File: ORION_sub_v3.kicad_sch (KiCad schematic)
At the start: 74 parts, among them J1 Conn_01x02, J10 Conn_01x01, J11 Conn_01x05, J12 Conn_01x04, J2 Conn_01x03, J3 Conn_01x04, J4 Conn_01x02, J5 Conn_01x01, J6 Conn_01x04, J7 Conn_01x03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

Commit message: スイッチ変更、電源ヒューズ追加
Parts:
- added F1: Polyfuse, Fuse:Fuse_1206_3216Metric, symbol Device:Polyfuse
- SW1, SW2, SW3, SW4: footprint Button_Switch_SMD:SW_Push_1P1T_NO_CK_KMR2 -> Button_Switch_SMD:SW_Push_SPST_NO_Alps_SKRK
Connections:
- net +BATT: now also F1.1; no longer C12.1, U4.4 (EN), U4.5 (VCC)
- new net BATT_fuse: C12.1, F1.2, U4.4 (EN), U4.5 (VCC)
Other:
- note added: "要修正"
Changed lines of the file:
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@@
   (junction (at 62.23 163.83) (diameter 0) (color 0 0 0 0)
   )
-  (junction (at 54.61 168.91) (diameter 0) (color 0 0 0 0)
-  )
   (junction (at 49.53 115.57) (diameter 0) (color 0 0 0 0)
   )
@@
     (stroke (width 0) (type default) (color 0 0 0 0))
   )
+  (wire (pts (xy 48.26 167.64) (xy 48.26 168.91))
+    (stroke (width 0) (type default) (color 0 0 0 0))
+  )
   (wire (pts (xy 81.28 173.99) (xy 88.9 173.99))
     (stroke (width 0) (type default) (color 0 0 0 0))
@@
     (stroke (width 0) (type default) (color 0 0 0 0))
   )
+  (wire (pts (xy 31.75 137.16) (xy 38.1 137.16))
+    (stroke (width 0) (type default) (color 0 0 0 0))
+  )
   (wire (pts (xy 33.02 182.88) (xy 27.94 182.88))
     (stroke (width 0) (type default) (color 0 0 0 0))
@@
     (stroke (width 0) (type default) (color 0 0 0 0))
   )
+  (wire (pts (xy 45.72 137.16) (xy 49.53 137.16))
+    (stroke (width 0) (type default) (color 0 0 0 0))
+  )
   (wire (pts (xy 162.56 16.51) (xy 165.1 16.51))
     (stroke (width 0) (type default) (color 0 0 0 0))
@@
     (stroke (width 0) (type default) (color 0 0 0 0))
   )
+  (text "要修正" (at 123.19 198.12 0)
+    (effects (font (size 5 5)) (justify left bottom))
+  )
   (label "SW_0" (at 123.19 20.32 180)
     (effects (font (size 1.27 1.27)) (justify right bottom))
@@
     (effects (font (size 1.27 1.27)) (justify right bottom))
   )
+  (label "BATT_fuse" (at 49.53 137.16 0)
+    (effects (font (size 1.27 1.27)) (justify left bottom))
+  )
   (label "OSC_OUT" (at 236.22 20.32 0)
     (effects (font (size 1.524 1.524)) (justify left bottom))
@@
     (effects (font (size 1.27 1.27)) (justify right bottom))
   )
+  (label "BATT_fuse" (at 48.26 167.64 0)
+    (effects (font (size 1.27 1.27)) (justify left bottom))
+  )
   (label "LED_2" (at 34.29 64.77 180)
     (effects (font (size 1.524 1.524)) (justify right bottom))
@@
       (effects (font (size 1.27 1.27)) (justify right))
     )
-    (property "Footprint" "Button_Switch_SMD:SW_Push_1P1T_NO_CK_KMR2" (id 2) (at 130.81 25.4 0)
+    (property "Footprint" "Button_Switch_SMD:SW_Push_SPST_NO_Alps_SKRK" (id 2) (at 130.81 25.4 0)
       (effects (font (size 1.27 1.27)) hide)
     )
@@
       (effects (font (size 1.27 1.27)) (justify right))
     )
-    (property "Footprint" "Button_Switch_SMD:SW_Push_1P1T_NO_CK_KMR2" (id 2) (at 143.51 25.4 0)
+    (property "Footprint" "Button_Switch_SMD:SW_Push_SPST_NO_Alps_SKRK" (id 2) (at 143.51 25.4 0)
       (effects (font (size 1.27 1.27)) hide)
     )
@@
     (pin "1")
   )
+  (symbol (lib_id "Device:Polyfuse") (at 41.91 137.16 90) (unit 1)
+    (in_bom yes) (on_board yes) (fields_autoplaced)
+    (property "Reference" "F1" (id 0) (at 40.6399 134.62 0)
+      (effects (font (size 1.27 1.27)) (justify left))
+    )
+    (property "Value" "Polyfuse" (id 1) (at 43.1799 134.62 0)
+      (effects (font (size 1.27 1.27)) (justify left))
+    )
+    (property "Footprint" "Fuse:Fuse_1206_3216Metric" (id 2) (at 46.99 135.89 0)
+      (effects (font (size 1.27 1.27)) (justify left) hide)
+    )
+    (property "Datasheet" "~" (id 3) (at 41.91 137.16 0)
+      (effects (font (size 1.27 1.27)) hide)
+    )
+    (pin "1")
+    (pin "2")
+  )
   (symbol (lib_id "User:BD9G101G") (at 36.83 168.91 0) (unit 1)
     (in_bom yes) (on_board yes) (fields_autoplaced)
@@
       (effects (font (size 1.27 1.27)) (justify right))
     )
-    (property "Footprint" "Button_Switch_SMD:SW_Push_1P1T_NO_CK_KMR2" (id 2) (at 118.11 25.4 0)
+    (property "Footprint" "Button_Switch_SMD:SW_Push_SPST_NO_Alps_SKRK" (id 2) (at 118.11 25.4 0)
       (effects (font (size 1.27 1.27)) hide)
     )
@@
     (pin "1")
   )
-  (symbol (lib_id "power:+BATT") (at 54.61 168.91 0) (unit 1)
+  (symbol (lib_id "power:+BATT") (at 31.75 137.16 0) (unit 1)
     (in_bom yes) (on_board yes)
-    (property "Reference" "#PWR012" (id 0) (at 54.61 172.72 0)
+    (property "Reference" "#PWR012" (id 0) (at 31.75 140.97 0)
       (effects (font (size 1.27 1.27)) hide)
     )
-    (property "Value" "+BATT" (id 1) (at 48.26 166.37 0)
+    (property "Value" "+BATT" (id 1) (at 25.4 134.62 0)
       (effects (font (size 1.27 1.27)) (justify left))
     )
-    (property "Footprint" "" (id 2) (at 54.61 168.91 0)
+    (property "Footprint" "" (id 2) (at 31.75 137.16 0)
       (effects (font (size 1.27 1.27)) hide)
     )
-    (property "Datasheet" "" (id 3) (at 54.61 168.91 0)
+    (property "Datasheet" "" (id 3) (at 31.75 137.16 0)
       (effects (font (size 1.27 1.27)) hide)
     )
@@
     )
     (property "Value" "SW_Push" (id 1) (at 161.036 24.13 0))
-    (property "Footprint" "Button_Switch_SMD:SW_Push_1P1T_NO_CK_KMR2" (id 2) (at 167.64 24.13 0)
+    (property "Footprint" "Button_Switch_SMD:SW_Push_SPST_NO_Alps_SKRK" (id 2) (at 167.64 24.13 0)
       (effects (font (size 1.27 1.27)) hide)
     )
@@
       (reference "D10") (unit 1) (value "LED") (footprint "LED_SMD:LED_0603_1608Metric")
     )
+    (path "/42055cd1-520a-46d4-8bb1-032d7acd9f1c"
+      (reference "F1") (unit 1) (value "Polyfuse") (footprint "Fuse:Fuse_1206_3216Metric")
+    )
     (path "/b6763645-6ebb-43f8-9e23-2738718aabe3"
       (reference "J1") (unit 1) (value "Conn_01x02") (footprint "Connector_Hirose:Hirose_DF13-02P-1.25DSA_1x02_P1.25mm_Vertical")
@@
     )
     (path "/e2c39e4b-8894-40d7-8b0a-a70128ca8812"
-      (reference "SW1") (unit 1) (value "SW_Push") (footprint "Button_Switch_SMD:SW_Push_1P1T_NO_CK_KMR2")
+      (reference "SW1") (unit 1) (value "SW_Push") (footprint "Button_Switch_SMD:SW_Push_SPST_NO_Alps_SKRK")
     )
     (path "/ae53bb4e-83e0-4f31-8b54-9513ada53cca"
-      (reference "SW2") (unit 1) (value "SW_Push") (footprint "Button_Switch_SMD:SW_Push_1P1T_NO_CK_KMR2")
+      (reference "SW2") (unit 1) (value "SW_Push") (footprint "Button_Switch_SMD:SW_Push_SPST_NO_Alps_SKRK")
     )
     (path "/1c7c0e3b-07ed-4d05-9bda-8a1656c2d04b"
-      (reference "SW3") (unit 1) (value "SW_Push") (footprint "Button_Switch_SMD:SW_Push_1P1T_NO_CK_KMR2")
+      (reference "SW3") (unit 1) (value "SW_Push") (footprint "Button_Switch_SMD:SW_Push_SPST_NO_Alps_SKRK")
     )
     (path "/3fe8974f-82c8-4bf4-9d5e-55518adc24c7"
-      (reference "SW4") (unit 1) (value "SW_Push") (footprint "Button_Switch_SMD:SW_Push_1P1T_NO_CK_KMR2")
+      (reference "SW4") (unit 1) (value "SW_Push") (footprint "Button_Switch_SMD:SW_Push_SPST_NO_Alps_SKRK")
     )
     (path "/50c41588-ebff-4aa2-b689-dd60a441b123"

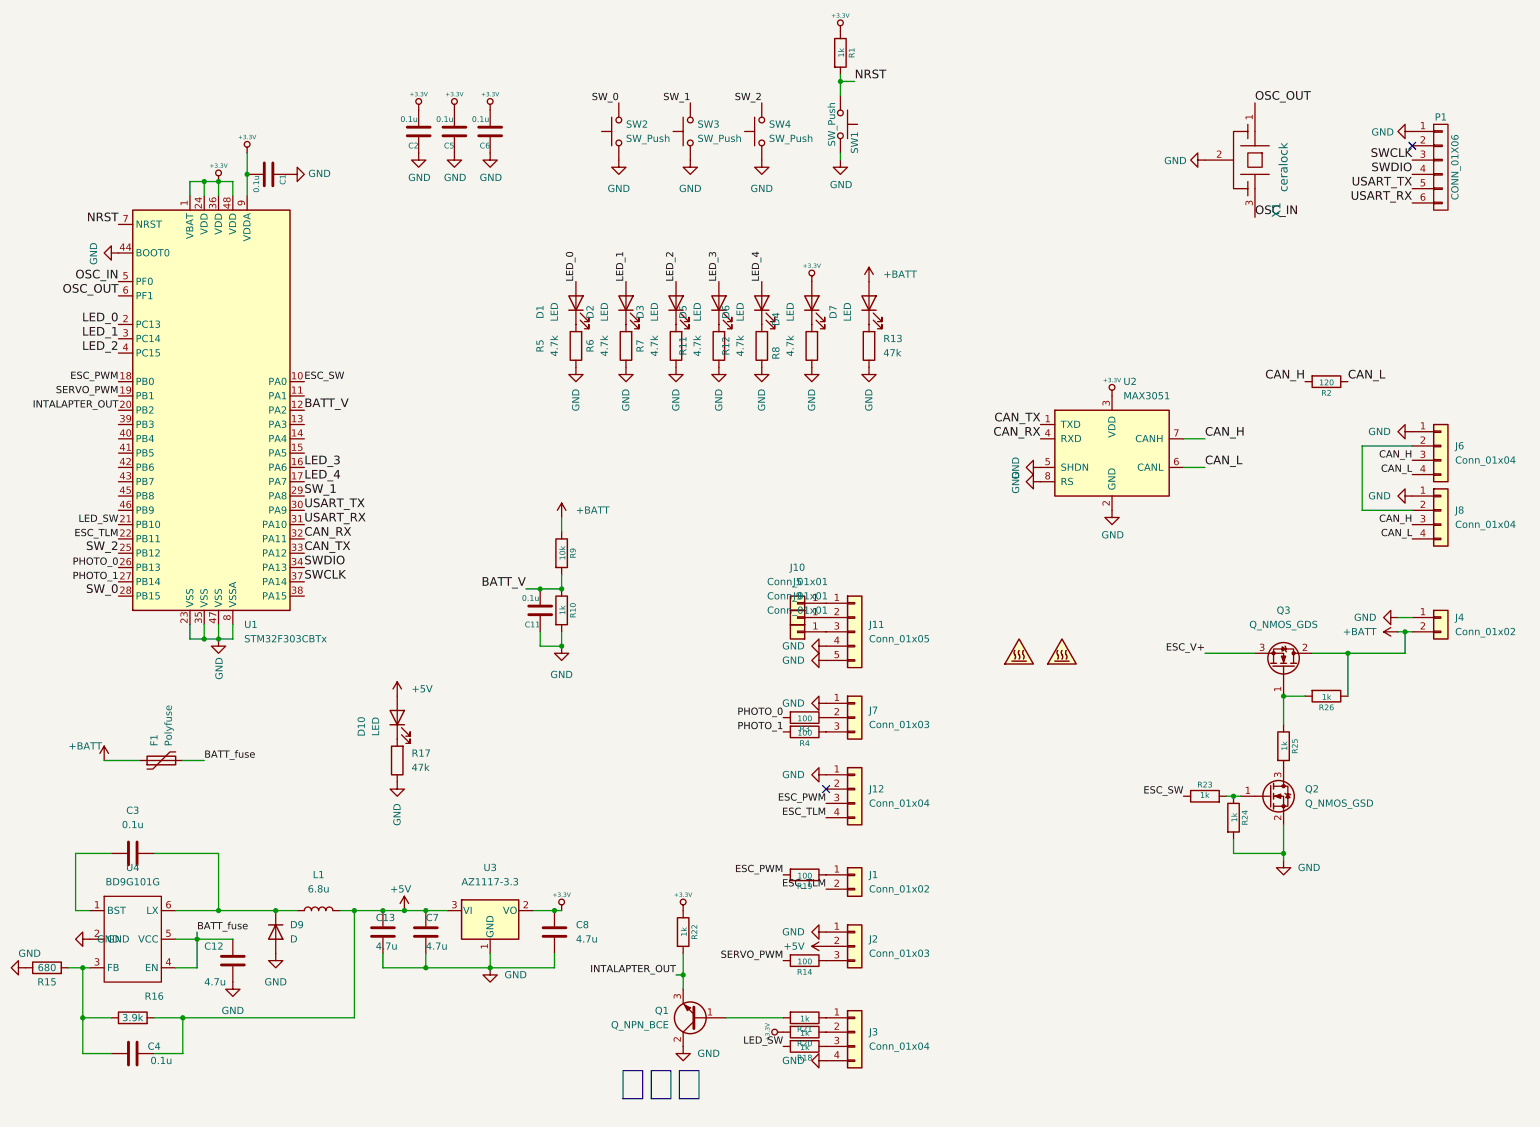
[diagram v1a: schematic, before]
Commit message: KiCAD8.0に更新
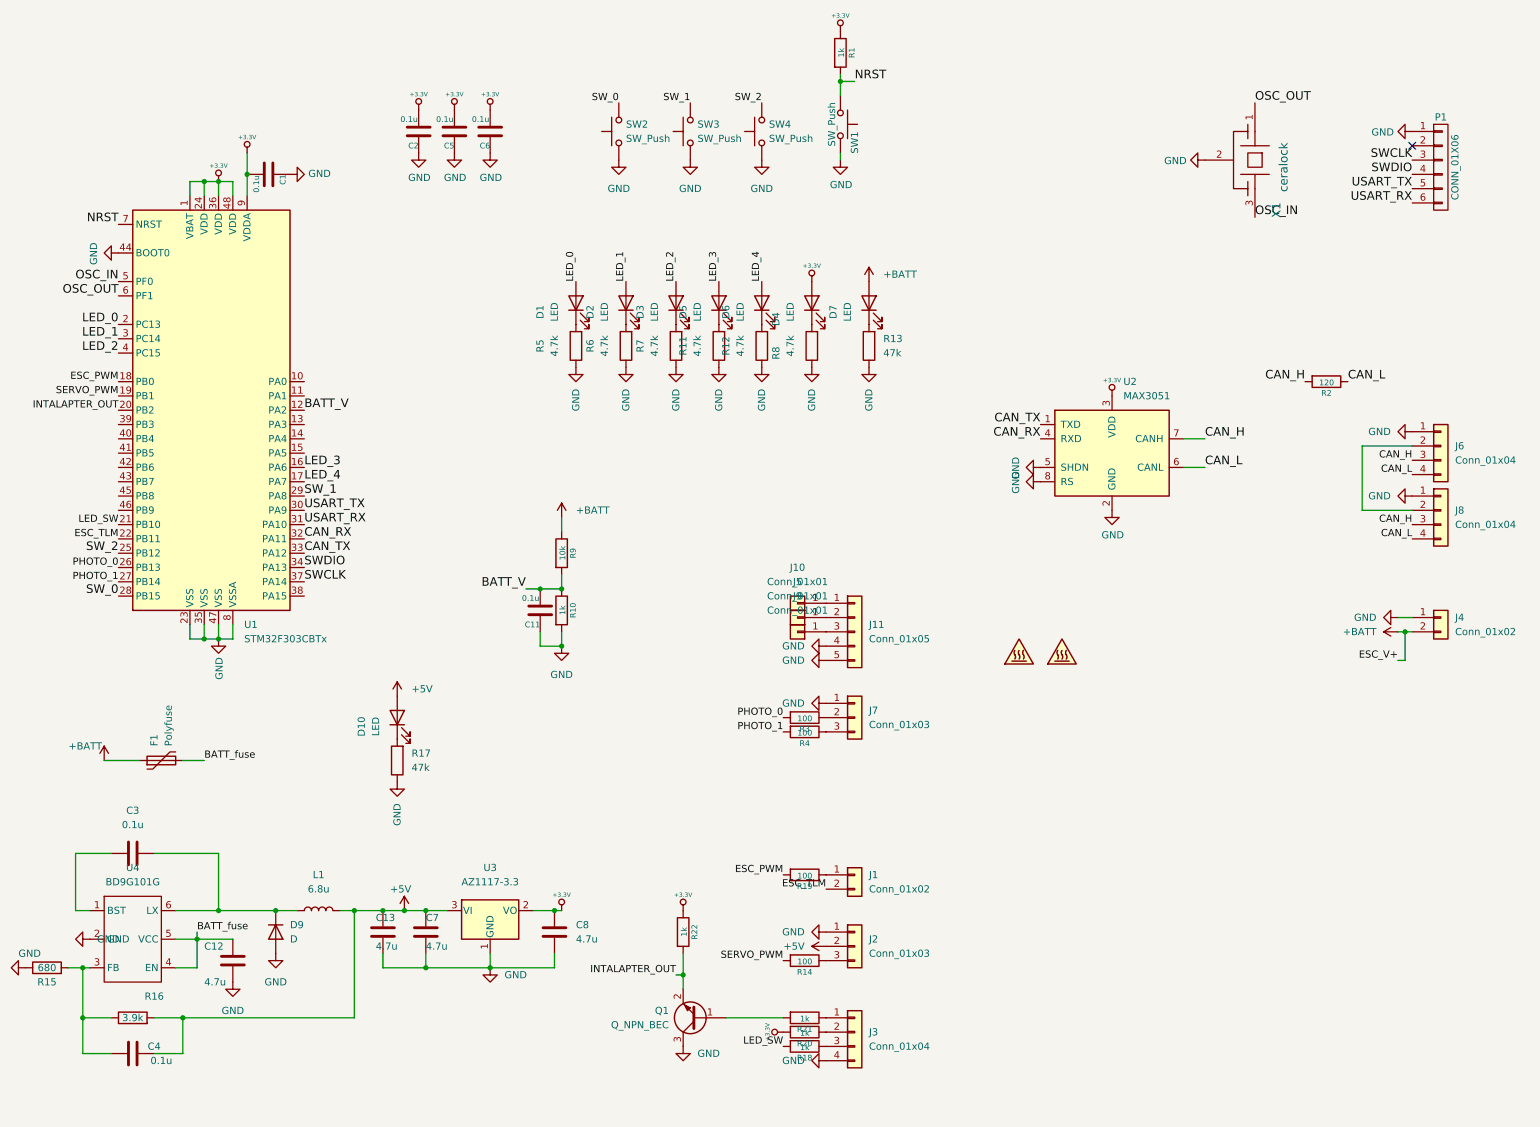
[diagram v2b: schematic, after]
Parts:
- removed J12: Conn_01x04, Connector_PinHeader_2.54mm:PinHeader_1x04_P2.54mm_Vertical, symbol Connector_Generic:Conn_01x04
- removed Q1: Q_NPN_BCE, Package_TO_SOT_SMD:SOT-23, symbol Device:Q_NPN_BCE
- removed Q2: Q_NMOS_GSD, Package_TO_SOT_SMD:SOT-23, symbol Device:Q_NMOS_GSD
- removed Q3: Q_NMOS_GDS, Package_TO_SOT_SMD:TO-252-2, symbol Device:Q_NMOS_GDS
- removed R23, R24, R25, R26: 1k, Resistor_SMD:R_0603_1608Metric, symbol SSL_BST_ver1.3-rescue:R
- added Q1: Q_NPN_BEC, Package_TO_SOT_SMD:SOT-23, symbol Device:Q_NPN_BEC
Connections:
- net GND: now also Q1.3 (C)
- net INTALAPTER_OUT: now also Q1.2 (E)
- net at R21.2: now also Q1.1 (B)
- net ESC_SW: no longer names the net of U1.10 (PA0)
- no-connect marks 2 -> 1
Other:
- note removed: "要修正"

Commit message: OLED追加
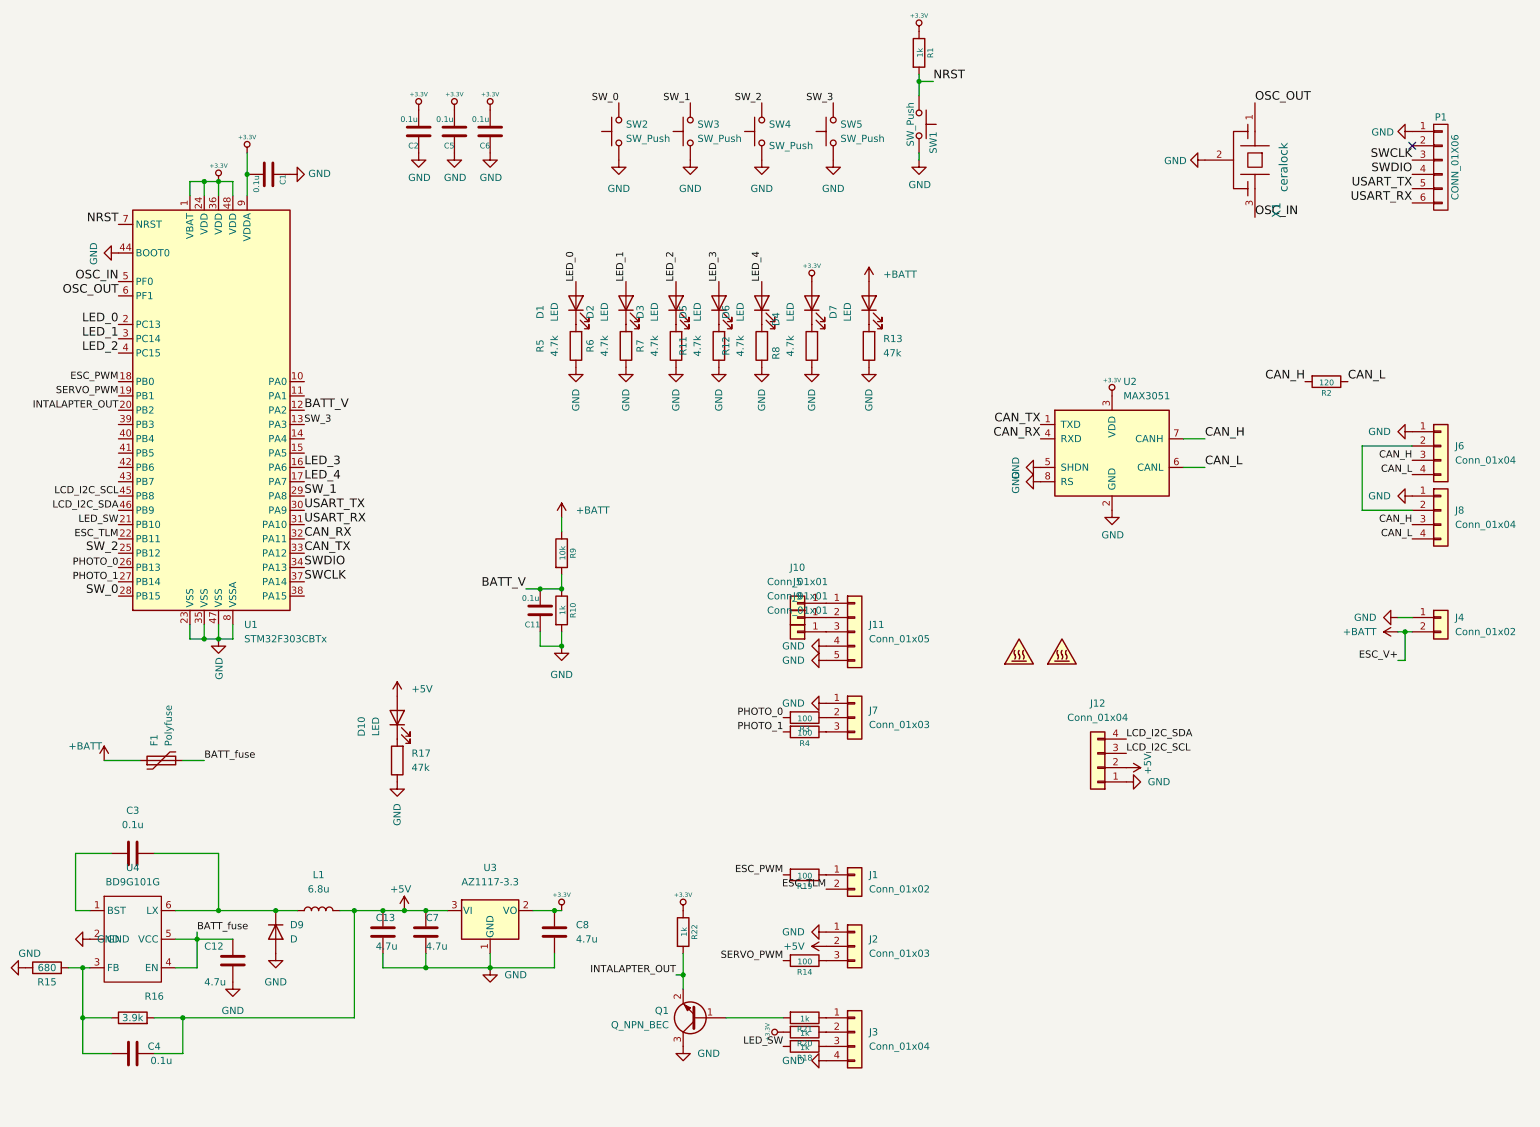
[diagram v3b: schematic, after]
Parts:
- added J12: Conn_01x04, Connector_PinHeader_2.54mm:PinHeader_1x04_P2.54mm_Vertical, symbol Connector_Generic:Conn_01x04
- added SW5: SW_Push, Button_Switch_SMD:SW_Push_SPST_NO_Alps_SKRK, symbol Switch:SW_Push
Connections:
- net +5V: now also J12.2 (Pin_2)
- net GND: now also J12.1 (Pin_1), SW5.1
- net SW_3: now reaches U1.13 (PA3)
- net SW_3: now also SW5.2
- net LCD_I2C_SCL: now reaches U1.45 (PB8)
- net LCD_I2C_SCL: now also J12.3 (Pin_3)
- net LCD_I2C_SDA: now reaches U1.46 (PB9)
- net LCD_I2C_SDA: now also J12.4 (Pin_4)
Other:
- moved on the sheet: R1, SW1

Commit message: 発注
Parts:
- removed Q1: Q_NPN_BEC, Package_TO_SOT_SMD:SOT-23, symbol Device:Q_NPN_BEC
- added Q1: 2SC4213, Package_TO_SOT_SMD:SOT-23, symbol Transistor_BJT:2SC4213
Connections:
- net GND: now also Q1.2 (E)
- net INTALAPTER_OUT: now also Q1.3 (C)
- net at R21.2: now also Q1.1 (B)
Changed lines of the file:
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@@
 	)
 	(symbol
+		(lib_id "Transistor_BJT:2SC4213")
+		(at 137.16 182.88 0)
+		(mirror y)
+		(unit 1)
+		(exclude_from_sim no)
+		(in_bom yes)
+		(on_board yes)
+		(dnp no)
+		(property "Reference" "Q1"
+			(at 132.08 181.6099 0)
+			(effects
+				(font
+					(size 1.27 1.27)
+				)
+				(justify left)
+			)
+		)
+		(property "Value" "2SC4213"
+			(at 132.08 184.1499 0)
+			(effects
+				(font
+					(size 1.27 1.27)
+				)
+				(justify left)
+			)
+		)
+		(property "Footprint" "Package_TO_SOT_SMD:SOT-23"
+			(at 132.08 184.785 0)
+			(effects
+				(font
+					(size 1.27 1.27)
+					(italic yes)
+				)
+				(justify left)
+				(hide yes)
+			)
+		)
+		(property "Datasheet" "https://toshiba.semicon-storage.com/info/docget.jsp?did=19305&prodName=2SC4213"
+			(at 137.16 182.88 0)
+			(effects
+				(font
+					(size 1.27 1.27)
+				)
+				(justify left)
+				(hide yes)
+			)
+		)
+		(property "Description" "0.3A Ic, 20V Vce, NPN Transistor, For Muting and Switching, SOT-323"
+			(at 137.16 182.88 0)
+			(effects
+				(font
+					(size 1.27 1.27)
+				)
+				(hide yes)
+			)
+		)
+		(pin "2"
+		)
+		(pin "1"
+		)
+		(pin "3"
+		)
+		(instances
+			(project ""
+				(path "/593597b3-baf3-4b6c-8937-40337314f8ae"
+					(reference "Q1")
+					(unit 1)
+				)
+			)
+		)
+	)
+	(symbol
 		(lib_id "SSL_BST_ver1.3-rescue:R")
 		(at 134.62 167.64 0)
@@
 					(unit 1)
 				)
-			)
-		)
-	)
-	(symbol
-		(lib_id "Device:Q_NPN_BEC")
-		(at 137.16 182.88 180)
-		(unit 1)
-		(exclude_from_sim no)
-		(in_bom yes)
-		(on_board yes)
-		(dnp no)
-		(fields_autoplaced yes)
-		(property "Reference" "Q1"
-			(at 132.08 181.6099 0)
-			(effects
-				(font
-					(size 1.27 1.27)
-				)
-				(justify left)
-			)
-		)
-		(property "Value" "Q_NPN_BEC"
-			(at 132.08 184.1499 0)
-			(effects
-				(font
-					(size 1.27 1.27)
-				)
-				(justify left)
-			)
-		)
-		(property "Footprint" "Package_TO_SOT_SMD:SOT-23"
-			(at 132.08 185.42 0)
-			(effects
-				(font
-					(size 1.27 1.27)
-				)
-				(hide yes)
-			)
-		)
-		(property "Datasheet" "~"
-			(at 137.16 182.88 0)
-			(effects
-				(font
-					(size 1.27 1.27)
-				)
-				(hide yes)
-			)
-		)
-		(property "Description" ""
-			(at 137.16 182.88 0)
-			(effects
-				(font
-					(size 1.27 1.27)
-				)
-				(hide yes)
-			)
-		)
-		(pin "1"
-		)
-		(pin "2"
-		)
-		(pin "3"
-		)
-		(instances
-			(project ""
-				(path "/593597b3-baf3-4b6c-8937-40337314f8ae"
-					(reference "Q1")
-					(unit 1)
-				)
